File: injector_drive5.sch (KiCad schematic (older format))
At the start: 17 parts, among them P34 CONN_1, P35 CONN_1, Q18 PIP-3104, Q19 HALL

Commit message: Removed LM1815 options. Now adaptive mode and square waves are the default,
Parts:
- C53: Field1 (none) -> newark,97M4148; Field2 (none) -> vendor1, smd w hem; Field3 (none) -> vendor2, thru w hem; Field4 (none) -> vendor2, smd w hem; Field5 (none) -> 200,V; Field6 (none) -> 10,%; Field7 (none) -> Multilayer Ceramic; Field8 (none) -> other,more,stuff
- D92, D95: Field1 (none) -> vendor1, thru w hem; Field2 (none) -> vendor1, smd w hem; Field3 (none) -> vendor2, thru w hem; Field4 (none) -> vendor2, smd w hem; Field5 (none) -> reverse,V; Field6 (none) -> current,A; Field7 (none) -> x; Field8 (none) -> other,more,stuff
- D93: Field1 (none) -> newark,18M3533; Field2 (none) -> vendor1, smd w hem; Field3 (none) -> vendor2, thru w hem; Field4 (none) -> vendor2, smd w hem; Field5 (none) -> 500,mW; Field6 (none) -> 20,mA; Field7 (none) -> X; Field8 (none) -> other,more,stuff
- D94: Field1 (none) -> newark,58K2469; Field2 (none) -> vendor1, smd w hem; Field3 (none) -> vendor2, thru w hem; Field4 (none) -> vendor2, smd w hem; Field5 (none) -> x,x; Field6 (none) -> x,x; Field7 (none) -> construct; Field8 (none) -> other,more,stuff
- L5: Field1 (none) -> vendor1, thru w hem; Field2 (none) -> vendor1, smd w hem; Field3 (none) -> vendor2, thru w hem; Field4 (none) -> vendor2, smd w hem; Field5 (none) -> x,x; Field6 (none) -> x,x; Field7 (none) -> x; Field8 (none) -> other,more,stuff
- Q18: Field1 (none) -> digi,PIP3104-ND; Field2 (none) -> vendor1, smd w hem; Field3 (none) -> vendor2, thru w hem; Field4 (none) -> vendor2, smd w hem; Field5 (none) -> 8,A; Field6 (none) -> x,x; Field7 (none) -> TOPFET; Field8 (none) -> other,more,stuff
- Q19: Field1 (none) -> digi,480-2002-ND; Field2 (none) -> vendor1, smd w hem; Field3 (none) -> vendor2, thru w hem; Field4 (none) -> vendor2, smd w hem; Field5 (none) -> x,x; Field6 (none) -> x,x; Field7 (none) -> x; Field8 (none) -> other,more,stuff
- R129: Field1 (none) -> newark,38k0327; Field2 (none) -> vendor1, smd w hem; Field3 (none) -> vendor2, thru w hem; Field4 (none) -> vendor2, smd w hem; Field5 (none) -> 250,mW; Field6 (none) -> 5,%; Field7 (none) -> carbon film; Field8 (none) -> other,more,stuff
- R130: Field1 (none) -> newark,38K0329; Field2 (none) -> vendor1, smd w hem; Field3 (none) -> vendor2, thru w hem; Field4 (none) -> vendor2, smd w hem; Field5 (none) -> 250,mW; Field6 (none) -> 5,%; Field7 (none) -> carbon film; Field8 (none) -> other,more,stuff
- R131: Field1 (none) -> newark,38k0352; Field2 (none) -> vendor1, smd w hem; Field3 (none) -> vendor2, thru w hem; Field4 (none) -> vendor2, smd w hem; Field5 (none) -> 250,mW; Field6 (none) -> 5,%; Field7 (none) -> carbon film; Field8 (none) -> other,more,stuff
- R132: Field1 (none) -> vendor1, thru w hem; Field2 (none) -> vendor1, smd w hem; Field3 (none) -> vendor2, thru w hem; Field4 (none) -> vendor2, smd w hem; Field5 (none) -> power,W; Field6 (none) -> tol,%; Field7 (none) -> construct; Field8 (none) -> other,more,stuff
- R133: Field1 (none) -> newark,38K0352; Field2 (none) -> vendor1, smd w hem; Field3 (none) -> vendor2, thru w hem; Field4 (none) -> vendor2, smd w hem; Field5 (none) -> 250,mW; Field6 (none) -> 5,%; Field7 (none) -> carbon film; Field8 (none) -> other,more,stuff
- R134: Field1 (none) -> newark,59K8561; Field2 (none) -> vendor1, smd w hem; Field3 (none) -> vendor2, thru w hem; Field4 (none) -> vendor2, smd w hem; Field5 (none) -> 1,W; Field6 (none) -> 5,%; Field7 (none) -> construct; Field8 (none) -> other,more,stuff
- R135: Field1 (none) -> newark,38K0340; Field2 (none) -> vendor1, smd w hem; Field3 (none) -> vendor2, thru w hem; Field4 (none) -> vendor2, smd w hem; Field5 (none) -> 1/4,W; Field6 (none) -> 5,%; Field7 (none) -> carbon film; Field8 (none) -> other,more,stuff

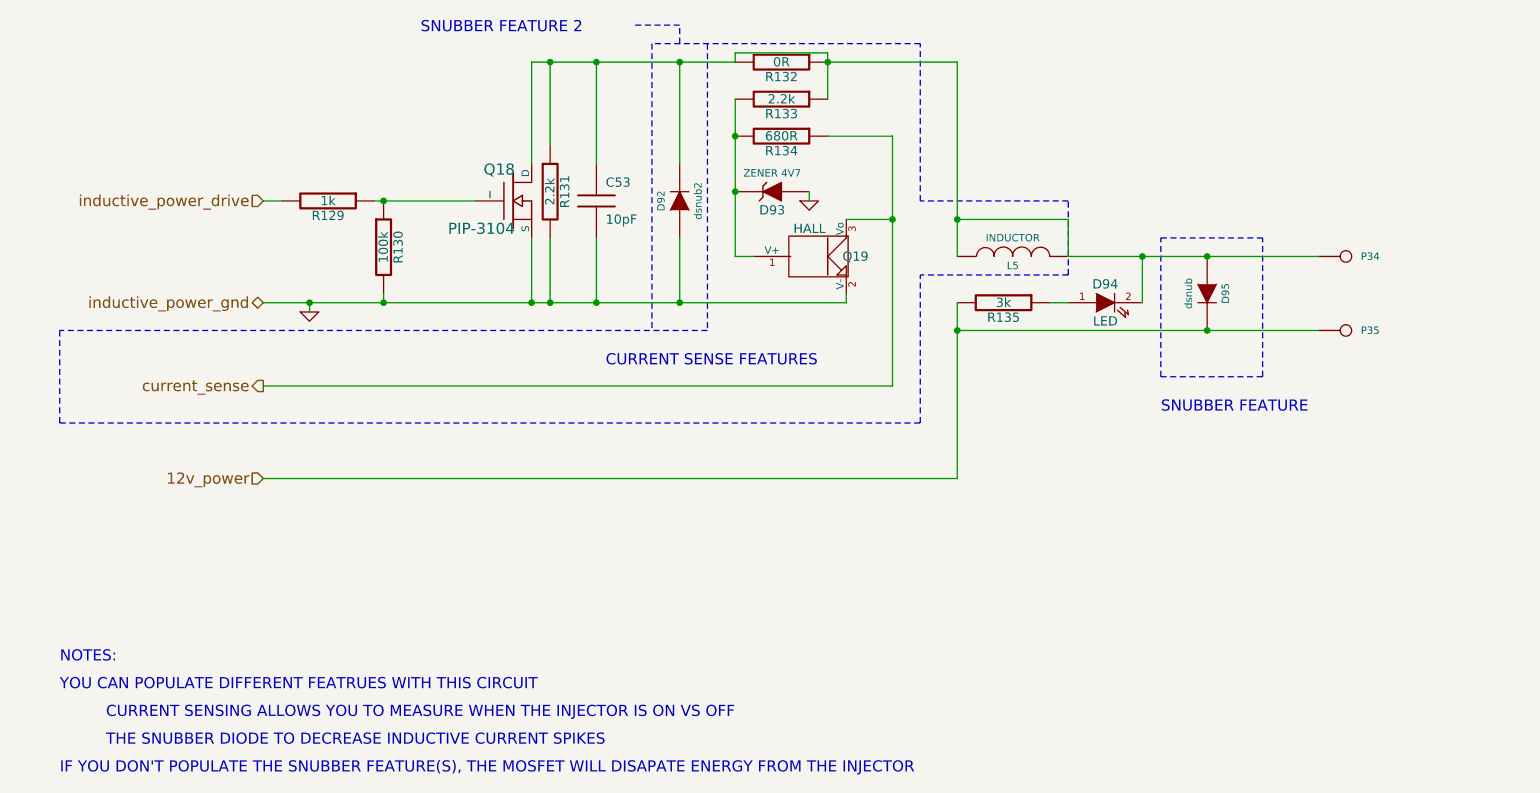
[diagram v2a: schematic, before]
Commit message: Implemented P&H, removed current sense circuitry, removed all unnecessary files from the repo
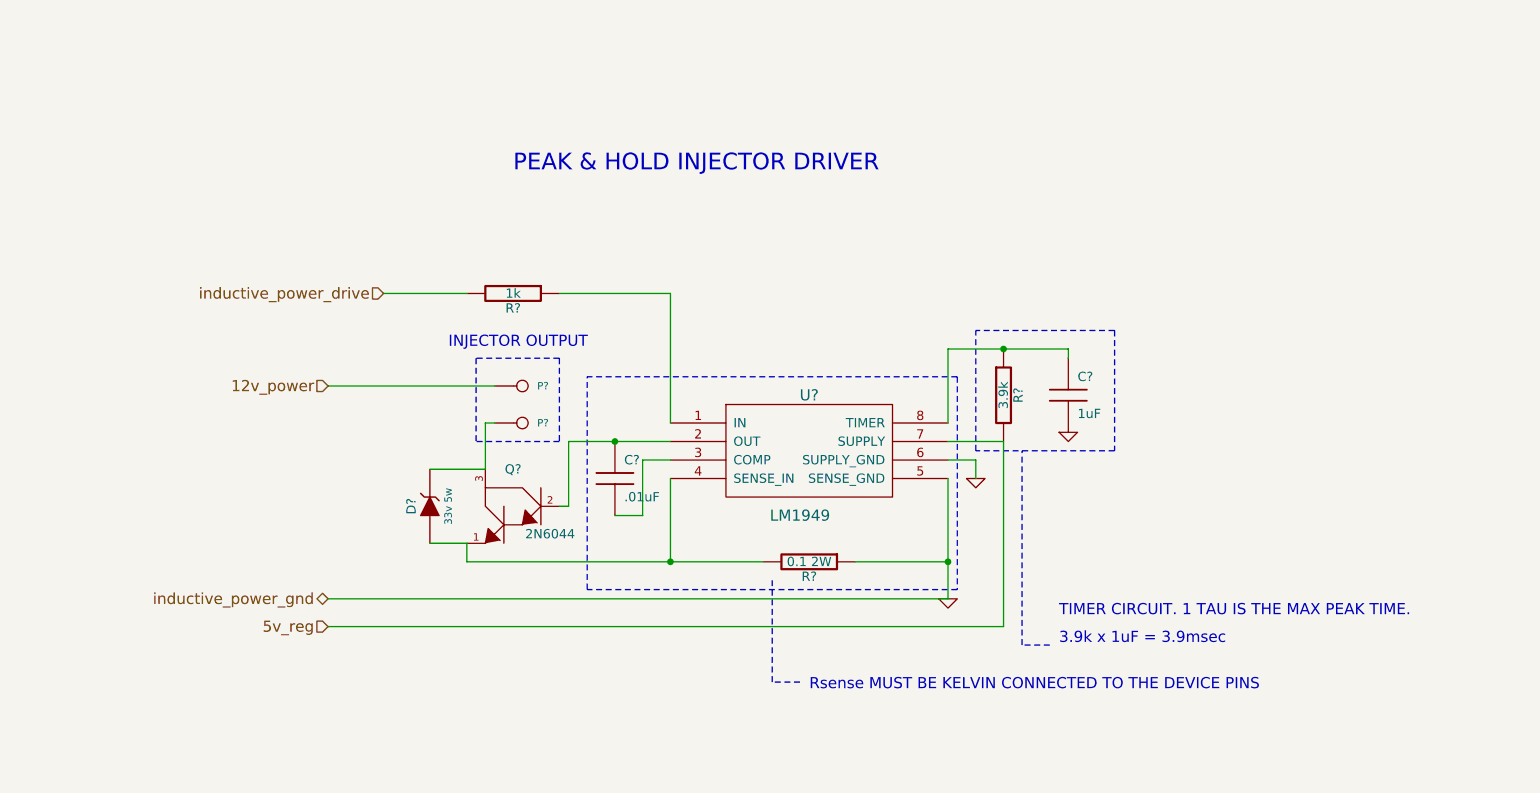
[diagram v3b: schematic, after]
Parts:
- removed C53: 10pF, C1V7, symbol C
- removed D92: dsnub2, D4-SMB, symbol DIODE
- removed D93: ZENER 4V7, D4-SMB, symbol ZENER
- removed D94: LED, LEDV, symbol LED
- removed D95: dsnub, D4-SMB, symbol DIODE
- removed L5: INDUCTOR, SIL-2, symbol INDUCTOR
- removed Q18: PIP-3104, TO220_sm, symbol PIP-3104
- removed Q19: HALL, SIL-3, symbol HALL
- removed R130: 100k, R4-SM0805, symbol R
- removed R131, R133: 2.2k, R4-SM0805, symbol R
- removed R132: 0R, R4-SM0805, symbol R
- removed R134: 680R, R4-SM0805, symbol R
- removed R135: 3k, R4-SM0805, symbol R
- added C?: .01uF, symbol C
- added C?: 1uF, symbol C
- added D?: 33v 5w, symbol ZENER
- added Q?: 2N6044, symbol DARL_N
- added R?: 0.1 2W, symbol R
- added R?: 3.9k, symbol R
- added U?: LM1949, DIP8, symbol LM1949
- renumbered P34 to P?, P35 to P?, R129 to R?
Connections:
- net 12v_power: now also P?.1; no longer P?.1
- net GND: now also C?.2, R?.1, U?.5 (SENSE_GND), U?.6 (SUPPLY_GND)
- net at R?.1: now also U?.1 (IN)
- new net: D?.2 (K), P?.1, Q?.3
- new net: C?.1, Q?.2, U?.2 (OUT)
- new net: C?.2, U?.3 (COMP)
- new net: D?.1 (A), Q?.1, R?.2, U?.4 (SENSE_IN)
- new net: C?.1, R?.1, U?.8 (TIMER)
- new net 5v_reg: R?.2, U?.7 (SUPPLY)
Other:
- note added: "3.9k x 1uF = 3.9msec"
- note added: "INJECTOR OUTPUT"
- note added: "PEAK & HOLD INJECTOR DRIVER"
- note added: "Rsense MUST BE KELVIN CONNECTED TO THE DEVICE PINS"
- note added: "TIMER CIRCUIT. 1 TAU IS THE MAX PEAK TIME."
- note removed: "CURRENT SENSE FEATURES"
- note removed: "CURRENT SENSING ALLOWS YOU TO MEASURE WHEN THE INJECTOR IS ON VS OFF"
- note removed: "IF YOU DON'T POPULATE THE SNUBBER FEATURE(S), THE MOSFET WILL DISAPATE ENERGY FROM THE INJECTOR"
- note removed: "NOTES:"
- note removed: "SNUBBER FEATURE"
- note removed: "SNUBBER FEATURE 2"
- note removed: "THE SNUBBER DIODE TO DECREASE INDUCTIVE CURRENT SPIKES"
- note removed: "YOU CAN POPULATE DIFFERENT FEATRUES WITH THIS CIRCUIT"
- moved on the sheet: P?, R?
